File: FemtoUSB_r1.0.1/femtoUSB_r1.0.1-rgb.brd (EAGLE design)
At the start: 20.7 x 15.2 mm, 34 parts, among them IC1 ATSAMD21E18A-MUT

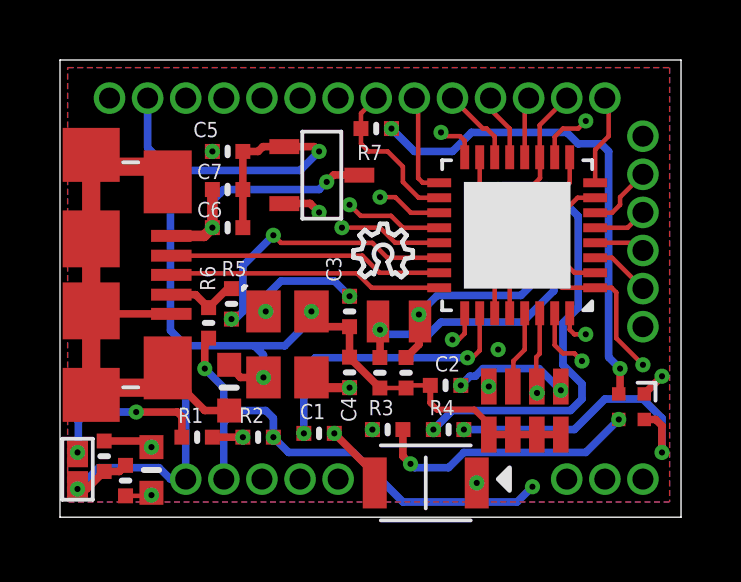
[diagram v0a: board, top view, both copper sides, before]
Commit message: Updating breadboard version. Adjusting USB ID pin connection back to PA28 on both FemtoUSB, and FemtoUSB breadboard layout
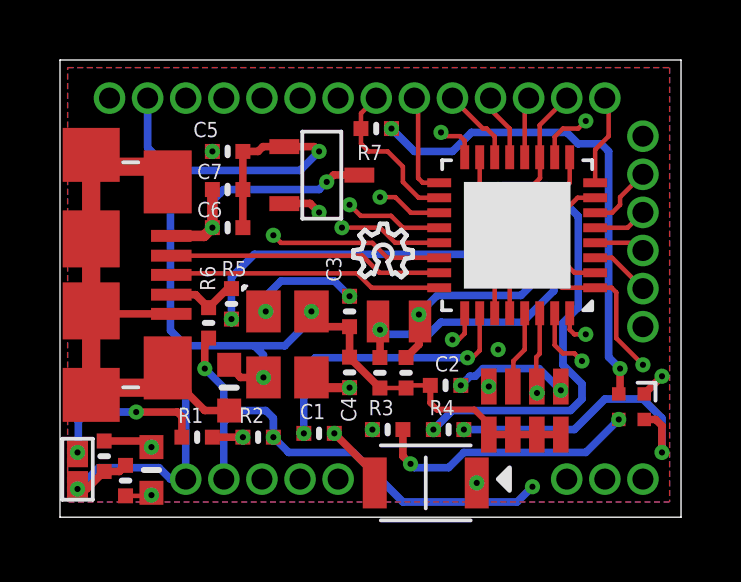
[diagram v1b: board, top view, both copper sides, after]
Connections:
- net PA23/USB/SOF1KHZ/I2C: no longer R5.2
- net PA28: now also R5.2
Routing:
- net PA28: track 11.6 -> 22.3 mm, vias 2 -> 3
- net PA23/USB/SOF1KHZ/I2C: track 14.5 -> 11.1 mm, vias 2 -> 1
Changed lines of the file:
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@@
 <wire x1="5.588" y1="12.7" x2="5.588" y2="13.843" width="0.254" layer="2"/>
 <wire x1="5.588" y1="13.843" x2="5.461" y2="13.97" width="0.254" layer="2"/>
-<contactref element="R5" pad="2"/>
-<via x="5.715" y="6.604" extent="1-16" drill="0.2032" diameter="0.508"/>
-<wire x1="5.715" y1="6.604" x2="5.842" y2="6.604" width="0.2032" layer="16"/>
-<wire x1="5.842" y1="6.604" x2="6.096" y2="6.858" width="0.254" layer="16"/>
-<wire x1="6.096" y1="6.858" x2="6.096" y2="8.382" width="0.254" layer="16"/>
-<wire x1="6.096" y1="8.382" x2="7.112" y2="9.398" width="0.254" layer="16"/>
 </signal>
 <signal name="PA24/USBDM">
@@
 <wire x1="17.526" y1="2.159" x2="18.161" y2="1.524" width="0.254" layer="2"/>
 <wire x1="18.161" y1="1.524" x2="18.161" y2="1.27" width="0.254" layer="2"/>
+<contactref element="R5" pad="2"/>
+<via x="5.715" y="6.604" extent="1-16" drill="0.2032" diameter="0.508"/>
+<wire x1="5.715" y1="6.604" x2="5.715" y2="8.001" width="0.254" layer="16"/>
+<wire x1="5.715" y1="8.001" x2="6.477" y2="8.763" width="0.254" layer="16"/>
+<wire x1="6.477" y1="8.763" x2="14.478" y2="8.763" width="0.254" layer="16"/>
+<wire x1="14.478" y1="8.763" x2="14.605" y2="8.89" width="0.254" layer="16"/>
 </signal>
 <signal name="VDDCORE">

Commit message: Updating FemtoUSB r1.0.1 w/ RGB. Silkscreen updated to reflect Arduino pin assignments
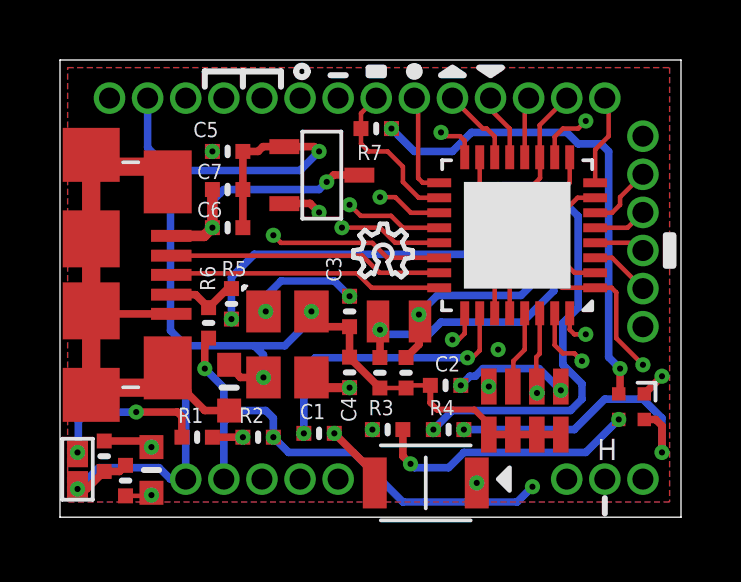
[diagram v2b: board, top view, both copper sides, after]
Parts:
- renumbered C_ARR1 to C_ARR, U$40 to OSC32K, U$43 to BTN_BOOT
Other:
- board text added: "A0"
- board text added: "A1"
- board text added: "A2"
- board text added: "A3"
- board text added: "A4"
- board text added: "AREF"
- board text added: "D2"
- board text added: "D22"
- board text added: "D3"
- board text added: "D4"
- board text added: "D5"
- board text added: "D6"
- board text added: "H"
- board text added: "MISO"
- board text added: "MOSI"
- board text added: "RX"
- board text added: "SCK"
- board text added: "SCL"
- board text added: "SDA"
- board text added: "SS"
- board text added: "SWCLK"
- board text added: "SWDIO"
- board text added: "TX"
- board text removed: "PA00"
- board text removed: "PA01"
- board text removed: "PA02"
- board text removed: "PA03/VREF"
- board text removed: "PA04"
- board text removed: "PA05"
- board text removed: "PA06"
- board text removed: "PA07"
- board text removed: "PA08"
- board text removed: "PA09"
- board text removed: "PA10"
- board text removed: "PA11"
- board text removed: "PA16"
- board text removed: "PA17"
- board text removed: "PA18"
- board text removed: "PA19"
- board text removed: "PA22"
- board text removed: "PA23"
- board text removed: "PA27"
- board text removed: "PA28"
- board text removed: "PA30/SWCLK"
- board text removed: "PA31/SWDIO"

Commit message: Updating cap value for 32.768KHz crystal to correct value, adding in example sketches
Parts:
- C10, C11: value 12pF -> 4pF
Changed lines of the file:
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@@
 <element name="C8" library="microbuilder" package="_0402MP" value="10uF" x="2.1844" y="1.2192" smashed="yes" rot="R270"/>
 <element name="OSC32K" library="crystals" package="ABS06-107-32.768KHZ-T" value="ABS06-107-32.768KHZ-T" x="11.3" y="6.5238"/>
-<element name="C10" library="microbuilder" package="_0402MP" value="12pF" x="10.6628" y="4.8148" smashed="yes" rot="R90"/>
-<element name="C11" library="microbuilder" package="_0402MP" value="12pF" x="11.534" y="4.8148" smashed="yes" rot="R90"/>
+<element name="C10" library="microbuilder" package="_0402MP" value="4pF" x="10.6628" y="4.8148" smashed="yes" rot="R90"/>
+<element name="C11" library="microbuilder" package="_0402MP" value="4pF" x="11.534" y="4.8148" smashed="yes" rot="R90"/>
 <element name="BTN_BOOT" library="omron_tactile_switch" package="SIDE_ACT_NO_GND_NO_BOSS" value="TACTILE_SWITCH_NO_GND_NO_BOSS" x="12.192" y="1.143" rot="R180"/>
 <element name="R5" library="microbuilder" package="_0402MP" value="330" x="5.715" y="7.112" smashed="yes" rot="R270">

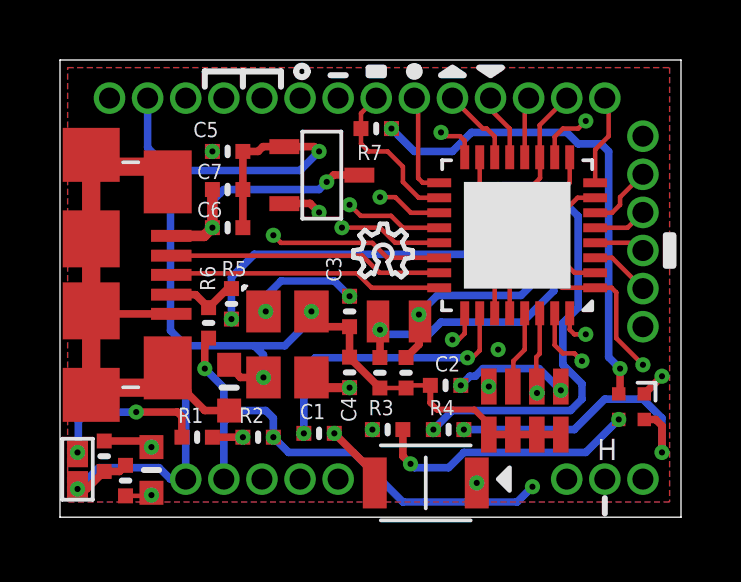
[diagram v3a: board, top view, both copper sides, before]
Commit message: Updating Bill of Materials, and component attributes to include mfr ID. Button is now used by PA27 instead of PA15 (boot), since Arduino core doesn't need the boot pin to upload subsequent sketches
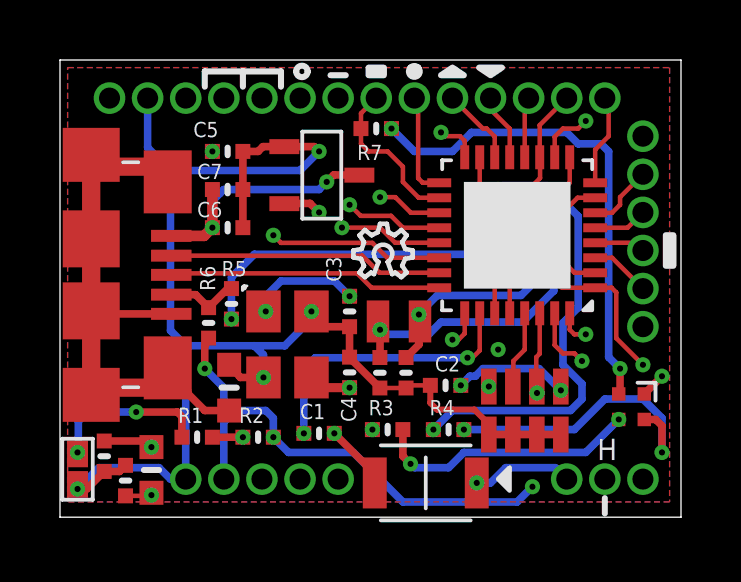
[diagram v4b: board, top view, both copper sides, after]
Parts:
- SJ_RESET: value OMRON B3U-300P(M) -> (none)
- renumbered U$12 to PIN_1X6, U$6 to PIN_1X14, U$7 to PIN_1X3, U$9 to PIN_1X5
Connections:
- net PA15/XOUT: no longer BTN_BOOT.1
- net PA27: now also BTN_BOOT.1
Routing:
- net PA15/XOUT: track 20.1 -> 13.1 mm, vias 3 -> 2
- net PA27: track 8.35 -> 11.7 mm, vias 1 -> 2

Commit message: Caps for 48MHz updated from 9pF to 10pF. Updated to correct manufacturor ID for too. Minor fix to skewed polygon - was supposed to be rectangular.
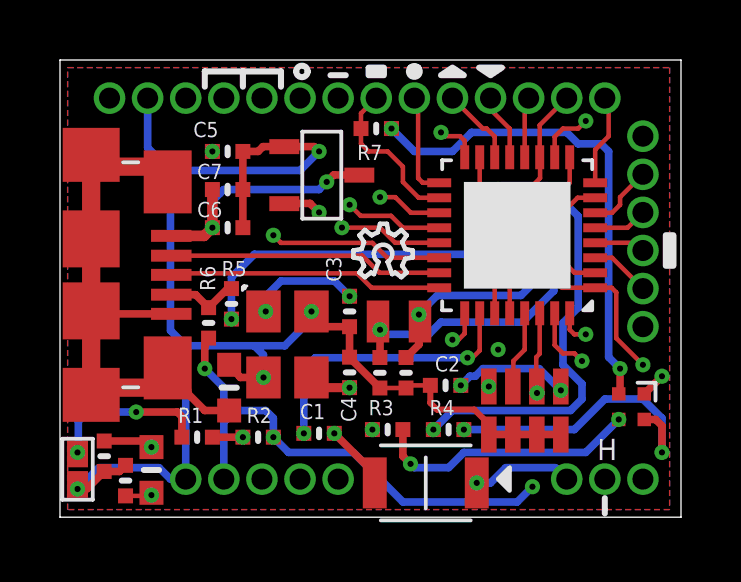
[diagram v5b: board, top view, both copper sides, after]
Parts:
- C3, C4: value 9pF -> 10pF
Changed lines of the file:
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@@
 <vertex x="20.447" y="9.398"/>
 </polygon>
+<dimension x1="0" y1="15.24" x2="20.701" y2="15.24" x3="10.3505" y3="16.51" textsize="1.778" layer="51" unit="inch" visible="yes"/>
+<dimension x1="20.701" y1="0" x2="20.701" y2="15.24" x3="24.13" y3="7.62" textsize="1.778" layer="51" unit="inch" visible="yes"/>
 </plain>
 <attributes>
@@
 <attribute name="MFR_ID" value="C1005X5R1A475K050BC" x="12.8524" y="4.3942" size="1.778" layer="27" rot="R180" display="off"/>
 </element>
-<element name="C3" library="microbuilder" package="_0402MP" value="9pF" x="9.652" y="6.858" smashed="yes" rot="R90">
+<element name="C3" library="microbuilder" package="_0402MP" value="10pF" x="9.652" y="6.858" smashed="yes" rot="R90">
 <attribute name="NAME" x="9.3789" y="7.8486" size="0.508" layer="25" font="vector" ratio="20" rot="R90"/>
-<attribute name="MFR_ID" value="GRM0335C1E100JA01D" x="9.652" y="6.858" size="1.778" layer="27" rot="R90" display="off"/>
-</element>
-<element name="C4" library="microbuilder" package="_0402MP" value="9pF" x="9.652" y="4.826" smashed="yes" rot="R270">
+<attribute name="MFR_ID" value="VJ0402A100FXACW1BC" x="9.652" y="6.858" size="1.778" layer="27" rot="R90" display="off"/>
+</element>
+<element name="C4" library="microbuilder" package="_0402MP" value="10pF" x="9.652" y="4.826" smashed="yes" rot="R270">
 <attribute name="NAME" x="9.3663" y="4.0132" size="0.508" layer="25" font="vector" ratio="20" rot="R270"/>
-<attribute name="MFR_ID" value="GRM0335C1E100JA01D" x="9.652" y="4.826" size="1.778" layer="27" rot="R270" display="off"/>
+<attribute name="MFR_ID" value="VJ0402A100FXACW1BC" x="9.652" y="4.826" size="1.778" layer="27" rot="R270" display="off"/>
 </element>
 <element name="R2" library="microbuilder" package="_0402MP" value="10K" x="6.604" y="2.667" smashed="yes">
-<attribute name="NAME" x="5.969" y="3.1433" size="0.508" layer="25" font="vector" ratio="20"/>
+<attribute name="NAME" x="6.223" y="3.1433" size="0.508" layer="25" font="vector" ratio="20"/>
 <attribute name="VALUE" x="5.969" y="1.8732" size="0.4572" layer="27" font="vector" ratio="20"/>
 <attribute name="MFR_ID" value="CRCW040210K0JNEDHP" x="6.604" y="2.667" size="1.778" layer="27" display="off"/>
@@
 <vertex x="0.254" y="14.986"/>
 <vertex x="20.32" y="14.986"/>
-<vertex x="20.32" y="0.508"/>
-<vertex x="0.254" y="0.508"/>
+<vertex x="20.32" y="0.254"/>
+<vertex x="0.254" y="0.254"/>
 </polygon>
 <polygon width="0.127" layer="1" isolate="0.254">
 <vertex x="0.254" y="14.986"/>
 <vertex x="20.32" y="14.986"/>
-<vertex x="20.32" y="0.508"/>
-<vertex x="0.254" y="0.508"/>
+<vertex x="20.32" y="0.254"/>
+<vertex x="0.254" y="0.254"/>
 </polygon>
 </signal>
